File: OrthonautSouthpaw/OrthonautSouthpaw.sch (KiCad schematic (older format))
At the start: 152 parts, among them K1 7, K10 3, K11 ., K12 Tab, K13 Esc, K14 L_Shift, K15 L_Ctrl, K16 Q, K17 A, K18 Z, K19 Win, K2 4, K20 W, K21 S, K22 X, K23 L_Alt, K24 E, K25 D, K26 C, K27 Lower, K28 R, K29 F, K3 1, K30 V, K31 Space, K32 T, K33 G, K34 B, K35 Y, K36 H, K37 N, K38 U, K39 J, K4 8, K40 M, K41 Enter, K42 I, K43 K, K44 ,, K45 Raise, K46 O, K47 L, K48 ., K49 R_Alt, K5 5, K50 P, K51 ;, K52 /, K53 Fn, K54 BackSpace, K55 ', K56 R_Shift, K57 Left, K58 Insert, K59 Delete, K6 2, K60 Up, K61 Down, K62 Home, K63 End, K64 Right, K7 0, K8 9, K9 6, SW1 SW_PUSH, U1 Elite-C

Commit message: finished v1 board designed
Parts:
- removed SW1: SW_PUSH, Keebio-Parts:SW_Tactile_SPST_Angled_MJTP1117, symbol keyboard_parts:SW_PUSH
- added D4: D, Keebio-Parts:Diode-dual, symbol Device:D
- added K4: 0, Keebio-Parts:MX_PCB_100H, symbol keyboard_parts:KEYSW
- D1, D2, D3: footprint Keebio-Parts:Diode -> Keebio-Parts:Diode-dual
- D10: renamed from D9; footprint Keebio-Parts:Diode -> Keebio-Parts:Diode-dual
- D11: renamed from D10; footprint Keebio-Parts:Diode -> Keebio-Parts:Diode-dual
- D12: renamed from D11; footprint Keebio-Parts:Diode -> Keebio-Parts:Diode-dual
- D13: renamed from D12; footprint Keebio-Parts:Diode -> Keebio-Parts:Diode-dual
- D14: renamed from D13; footprint Keebio-Parts:Diode -> Keebio-Parts:Diode-dual
- D15: renamed from D14; footprint Keebio-Parts:Diode -> Keebio-Parts:Diode-dual
- D16: renamed from D15; footprint Keebio-Parts:Diode -> Keebio-Parts:Diode-dual
- D17: renamed from D16; footprint Keebio-Parts:Diode -> Keebio-Parts:Diode-dual
- D18: renamed from D17; footprint Keebio-Parts:Diode -> Keebio-Parts:Diode-dual
- D19: renamed from D18; footprint Keebio-Parts:Diode -> Keebio-Parts:Diode-dual
- D20: renamed from D19; footprint Keebio-Parts:Diode -> Keebio-Parts:Diode-dual
- D21: renamed from D20; footprint Keebio-Parts:Diode -> Keebio-Parts:Diode-dual
- D22: renamed from D21; footprint Keebio-Parts:Diode -> Keebio-Parts:Diode-dual
- D23: renamed from D22; footprint Keebio-Parts:Diode -> Keebio-Parts:Diode-dual
- D24: renamed from D23; footprint Keebio-Parts:Diode -> Keebio-Parts:Diode-dual
- D25: renamed from D28; footprint Keebio-Parts:Diode -> Keebio-Parts:Diode-dual
- D26: renamed from D29; footprint Keebio-Parts:Diode -> Keebio-Parts:Diode-dual
- D27: renamed from D30; footprint Keebio-Parts:Diode -> Keebio-Parts:Diode-dual
- D28: renamed from D31; footprint Keebio-Parts:Diode -> Keebio-Parts:Diode-dual
- D29: renamed from D32; footprint Keebio-Parts:Diode -> Keebio-Parts:Diode-dual
- D30: renamed from D33; footprint Keebio-Parts:Diode -> Keebio-Parts:Diode-dual
- D31: renamed from D34; footprint Keebio-Parts:Diode -> Keebio-Parts:Diode-dual
- D32: renamed from D35; footprint Keebio-Parts:Diode -> Keebio-Parts:Diode-dual
- D33: renamed from D40; footprint Keebio-Parts:Diode -> Keebio-Parts:Diode-dual
- D34: renamed from D41; footprint Keebio-Parts:Diode -> Keebio-Parts:Diode-dual
- D35: renamed from D42; footprint Keebio-Parts:Diode -> Keebio-Parts:Diode-dual
- D36: renamed from D47; footprint Keebio-Parts:Diode -> Keebio-Parts:Diode-dual
- D37: renamed from D48; footprint Keebio-Parts:Diode -> Keebio-Parts:Diode-dual
- D38: renamed from D49; footprint Keebio-Parts:Diode -> Keebio-Parts:Diode-dual
- D39: renamed from D50; footprint Keebio-Parts:Diode -> Keebio-Parts:Diode-dual
- D40: renamed from D51; footprint Keebio-Parts:Diode -> Keebio-Parts:Diode-dual
- D41: renamed from D52; footprint Keebio-Parts:Diode -> Keebio-Parts:Diode-dual
- D42: renamed from D53; footprint Keebio-Parts:Diode -> Keebio-Parts:Diode-dual
- D43: renamed from D58; footprint Keebio-Parts:Diode -> Keebio-Parts:Diode-dual
- D44: renamed from D59; footprint Keebio-Parts:Diode -> Keebio-Parts:Diode-dual
- D45: renamed from D60; footprint Keebio-Parts:Diode -> Keebio-Parts:Diode-dual
- D46: renamed from D61; footprint Keebio-Parts:Diode -> Keebio-Parts:Diode-dual
- D47: renamed from D62; footprint Keebio-Parts:Diode -> Keebio-Parts:Diode-dual
- D48: renamed from D63; footprint Keebio-Parts:Diode -> Keebio-Parts:Diode-dual
- D49: renamed from D64; footprint Keebio-Parts:Diode -> Keebio-Parts:Diode-dual
- D5: renamed from D4; footprint Keebio-Parts:Diode -> Keebio-Parts:Diode-dual
- D50: renamed from D65; footprint Keebio-Parts:Diode -> Keebio-Parts:Diode-dual
- D51: renamed from D66; footprint Keebio-Parts:Diode -> Keebio-Parts:Diode-dual
- D52: renamed from D67; footprint Keebio-Parts:Diode -> Keebio-Parts:Diode-dual
- D53: renamed from D68; footprint Keebio-Parts:Diode -> Keebio-Parts:Diode-dual
- D54: renamed from D69; footprint Keebio-Parts:Diode -> Keebio-Parts:Diode-dual
- D55: renamed from D70; footprint Keebio-Parts:Diode -> Keebio-Parts:Diode-dual
- D56: renamed from D71; footprint Keebio-Parts:Diode -> Keebio-Parts:Diode-dual
- D57: renamed from D72; footprint Keebio-Parts:Diode -> Keebio-Parts:Diode-dual
- D58: renamed from D73; footprint Keebio-Parts:Diode -> Keebio-Parts:Diode-dual
- D59: renamed from D74; footprint Keebio-Parts:Diode -> Keebio-Parts:Diode-dual
- D6: renamed from D5; footprint Keebio-Parts:Diode -> Keebio-Parts:Diode-dual
- D60: renamed from D75; footprint Keebio-Parts:Diode -> Keebio-Parts:Diode-dual
- D61: renamed from D76; footprint Keebio-Parts:Diode -> Keebio-Parts:Diode-dual
- D62: renamed from D77; footprint Keebio-Parts:Diode -> Keebio-Parts:Diode-dual
- D63: renamed from D78; footprint Keebio-Parts:Diode -> Keebio-Parts:Diode-dual
- D64: renamed from D79; footprint Keebio-Parts:Diode -> Keebio-Parts:Diode-dual
- D65: renamed from D80; footprint Keebio-Parts:Diode -> Keebio-Parts:Diode-dual
- D7: renamed from D6; footprint Keebio-Parts:Diode -> Keebio-Parts:Diode-dual
- D8: renamed from D7; footprint Keebio-Parts:Diode -> Keebio-Parts:Diode-dual
- D9: renamed from D8; footprint Keebio-Parts:Diode -> Keebio-Parts:Diode-dual
- H1, H2: footprint Keebio-Parts:MountingHole -> keyboard_parts:Poker_side_edge_long
- H3, H4, H5, H6: footprint Keebio-Parts:MountingHole -> keyboard_parts:Poker_oval_hole
- K8: renamed from K7; value 0 -> 00
- renumbered D24 to D66, D25 to D67, D26 to D68, D27 to D69, D36 to D70, D37 to D71, D38 to D72, D39 to D73, D43 to D74, D44 to D75, D45 to D76, D46 to D77, D54 to D78, D55 to D79, D56 to D80, D57 to D81, K9 to K10, K10 to K11, K11 to K12, K12 to K13, K13 to K14, K14 to K15, K15 to K16, K16 to K17, K17 to K18, K18 to K19, K19 to K20, K20 to K21, K21 to K22, K22 to K23, K23 to K24, K24 to K25, K25 to K26, K26 to K27, K27 to K28, K28 to K29, K29 to K30, K30 to K31, K31 to K32, K32 to K33, K33 to K34, K34 to K35, K35 to K36, K36 to K37, K37 to K38, K38 to K39, K39 to K40, K40 to K41, K41 to K42, K42 to K43, K43 to K44, K44 to K45, K45 to K46, K46 to K47, K47 to K48, K48 to K49, K4 to K5, K49 to K50, K50 to K51, K51 to K52, K52 to K53, K53 to K54, K54 to K55, K55 to K56, K56 to K57, K57 to K58, K58 to K59, K5 to K6, K59 to K60, K60 to K61, K61 to K62, K62 to K63, K63 to K64, K64 to K65, K6 to K7, K8 to K9
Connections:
- net col0: now also K4.1
- net row3: now also D4.1 (K)
- new net: D4.2 (A), K4.2
- no-connect marks 3 -> 4
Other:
- moved on the sheet: D66, D67, D68, D69, D70, D71, D72, D73, D74, D75, D76, D77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

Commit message: ordered pcb. used swillkb for case design
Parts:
- added H7, H8: Hole, keyboard_parts:Poker_oval_hole, symbol keebio:Hole
- H1, H2: footprint keyboard_parts:Poker_side_edge_long -> keyboard_parts:Poker_oval_hole
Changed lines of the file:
@@
-$EndComp
-$Comp
-L keebio:Hole H2
-U 1 1 5CE95236
-P 3400 8700
-F 0 "H2" H 3586 8753 60  0000 L CNN
-F 1 "Hole" H 3586 8647 60  0000 L CNN
-F 2 "keyboard_parts:Poker_side_edge_long" H 3400 8700 60  0001 C CNN
-F 3 "" H 3400 8700 60  0001 C CNN
-	1    3400 8700
-	1    0    0    -1
 $EndComp
 $Comp
@@
 F 3 "" H 4150 8700 60  0001 C CNN
 	1    4150 8700
-	1    0    0    -1
-$EndComp
-$Comp
-L keebio:Hole H1
-U 1 1 5CE9537A
-P 3400 8250
-F 0 "H1" H 3586 8303 60  0000 L CNN
-F 1 "Hole" H 3586 8197 60  0000 L CNN
-F 2 "keyboard_parts:Poker_side_edge_long" H 3400 8250 60  0001 C CNN
-F 3 "" H 3400 8250 60  0001 C CNN
-	1    3400 8250
 	1    0    0    -1
 $EndComp
@@
 Connection ~ 1850 2600
 NoConn ~ 2500 6850
+$Comp
+L keebio:Hole H1
+U 1 1 5CE9B221
+P 3400 7700
+F 0 "H1" H 3586 7753 60  0000 L CNN
+F 1 "Hole" H 3586 7647 60  0000 L CNN
+F 2 "keyboard_parts:Poker_oval_hole" H 3400 7700 60  0001 C CNN
+F 3 "" H 3400 7700 60  0001 C CNN
+	1    3400 7700
+	1    0    0    -1
+$EndComp
+$Comp
+L keebio:Hole H8
+U 1 1 5CE9B227
+P 4150 7700
+F 0 "H8" H 4336 7753 60  0000 L CNN
+F 1 "Hole" H 4336 7647 60  0000 L CNN
+F 2 "keyboard_parts:Poker_oval_hole" H 4150 7700 60  0001 C CNN
+F 3 "" H 4150 7700 60  0001 C CNN
+	1    4150 7700
+	1    0    0    -1
+$EndComp
+$Comp
+L keebio:Hole H7
+U 1 1 5CE9B22D
+P 4150 7200
+F 0 "H7" H 4336 7253 60  0000 L CNN
+F 1 "Hole" H 4336 7147 60  0000 L CNN
+F 2 "keyboard_parts:Poker_oval_hole" H 4150 7200 60  0001 C CNN
+F 3 "" H 4150 7200 60  0001 C CNN
+	1    4150 7200
+	1    0    0    -1
+$EndComp
+$Comp
+L keebio:Hole H2
+U 1 1 5CE9B233
+P 4150 6750
+F 0 "H2" H 4336 6803 60  0000 L CNN
+F 1 "Hole" H 4336 6697 60  0000 L CNN
+F 2 "keyboard_parts:Poker_oval_hole" H 4150 6750 60  0001 C CNN
+F 3 "" H 4150 6750 60  0001 C CNN
+	1    4150 6750
+	1    0    0    -1
+$EndComp
 $EndSCHEMATC

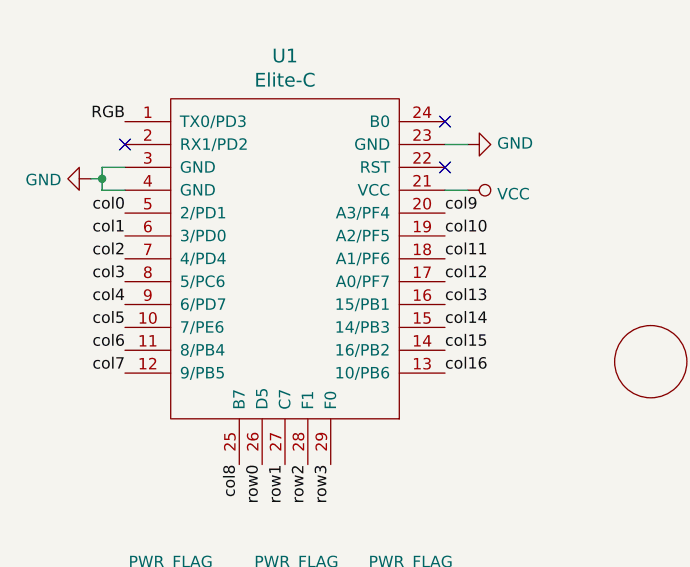
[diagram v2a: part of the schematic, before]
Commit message: update v2
v2 involves flipping the elitec component and moving it to have more space for the switch. arguably better tracing than v1
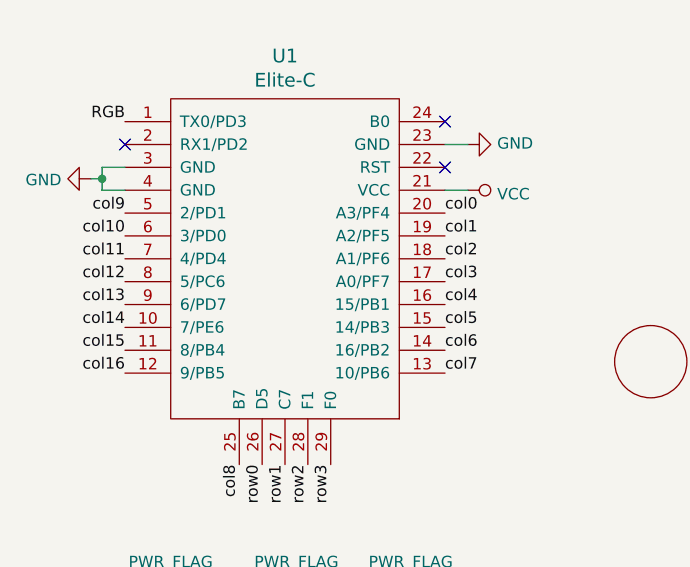
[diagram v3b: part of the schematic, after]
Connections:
- net col0: now also U1.20 (A3/PF4); no longer U1.5 (2/PD1)
- net col1: now also U1.19 (A2/PF5); no longer U1.6 (3/PD0)
- net col10: now also U1.6 (3/PD0); no longer U1.19 (A2/PF5)
- net col11: now also U1.7 (4/PD4); no longer U1.18 (A1/PF6)
- net col12: now also U1.8 (5/PC6); no longer U1.17 (A0/PF7)
- net col13: now also U1.9 (6/PD7); no longer U1.16 (15/PB1)
- net col14: now also U1.10 (7/PE6); no longer U1.15 (14/PB3)
- net col15: now also U1.11 (8/PB4); no longer U1.14 (16/PB2)
- net col16: now also U1.12 (9/PB5); no longer U1.13 (10/PB6)
- net col2: now also U1.18 (A1/PF6); no longer U1.7 (4/PD4)
- net col3: now also U1.17 (A0/PF7); no longer U1.8 (5/PC6)
- net col4: now also U1.16 (15/PB1); no longer U1.9 (6/PD7)
- net col5: now also U1.15 (14/PB3); no longer U1.10 (7/PE6)
- net col6: now also U1.14 (16/PB2); no longer U1.11 (8/PB4)
- net col7: now also U1.13 (10/PB6); no longer U1.12 (9/PB5)
- net col9: now also U1.5 (2/PD1); no longer U1.20 (A3/PF4)
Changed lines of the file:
@@
 Text Label 2000 8150 3    50   ~ 0
 row3
-Text Label 1100 7750 2    50   ~ 0
+Text Label 2500 7750 0    50   ~ 0
 col7
-Text Label 1100 7650 2    50   ~ 0
+Text Label 2500 7650 0    50   ~ 0
 col6
-Text Label 1100 7550 2    50   ~ 0
+Text Label 2500 7550 0    50   ~ 0
 col5
-Text Label 1100 7450 2    50   ~ 0
+Text Label 2500 7450 0    50   ~ 0
 col4
-Text Label 1100 7350 2    50   ~ 0
+Text Label 2500 7350 0    50   ~ 0
 col3
-Text Label 1100 7250 2    50   ~ 0
+Text Label 2500 7250 0    50   ~ 0
 col2
-Text Label 1100 7150 2    50   ~ 0
+Text Label 2500 7150 0    50   ~ 0
 col1
-Text Label 1100 7050 2    50   ~ 0
+Text Label 2500 7050 0    50   ~ 0
 col0
 Text Label 1600 8150 3    50   ~ 0
 col8
-Text Label 2500 7050 0    50   ~ 0
+Text Label 1100 7050 2    50   ~ 0
 col9
-Text Label 2500 7150 0    50   ~ 0
+Text Label 1100 7150 2    50   ~ 0
 col10
-Text Label 2500 7250 0    50   ~ 0
+Text Label 1100 7250 2    50   ~ 0
 col11
-Text Label 2500 7350 0    50   ~ 0
+Text Label 1100 7350 2    50   ~ 0
 col12
-Text Label 2500 7450 0    50   ~ 0
+Text Label 1100 7450 2    50   ~ 0
 col13
-Text Label 2500 7550 0    50   ~ 0
+Text Label 1100 7550 2    50   ~ 0
 col14
-Text Label 2500 7750 0    50   ~ 0
+Text Label 1100 7750 2    50   ~ 0
 col16
-Text Label 2500 7650 0    50   ~ 0
+Text Label 1100 7650 2    50   ~ 0
 col15
 $Comp

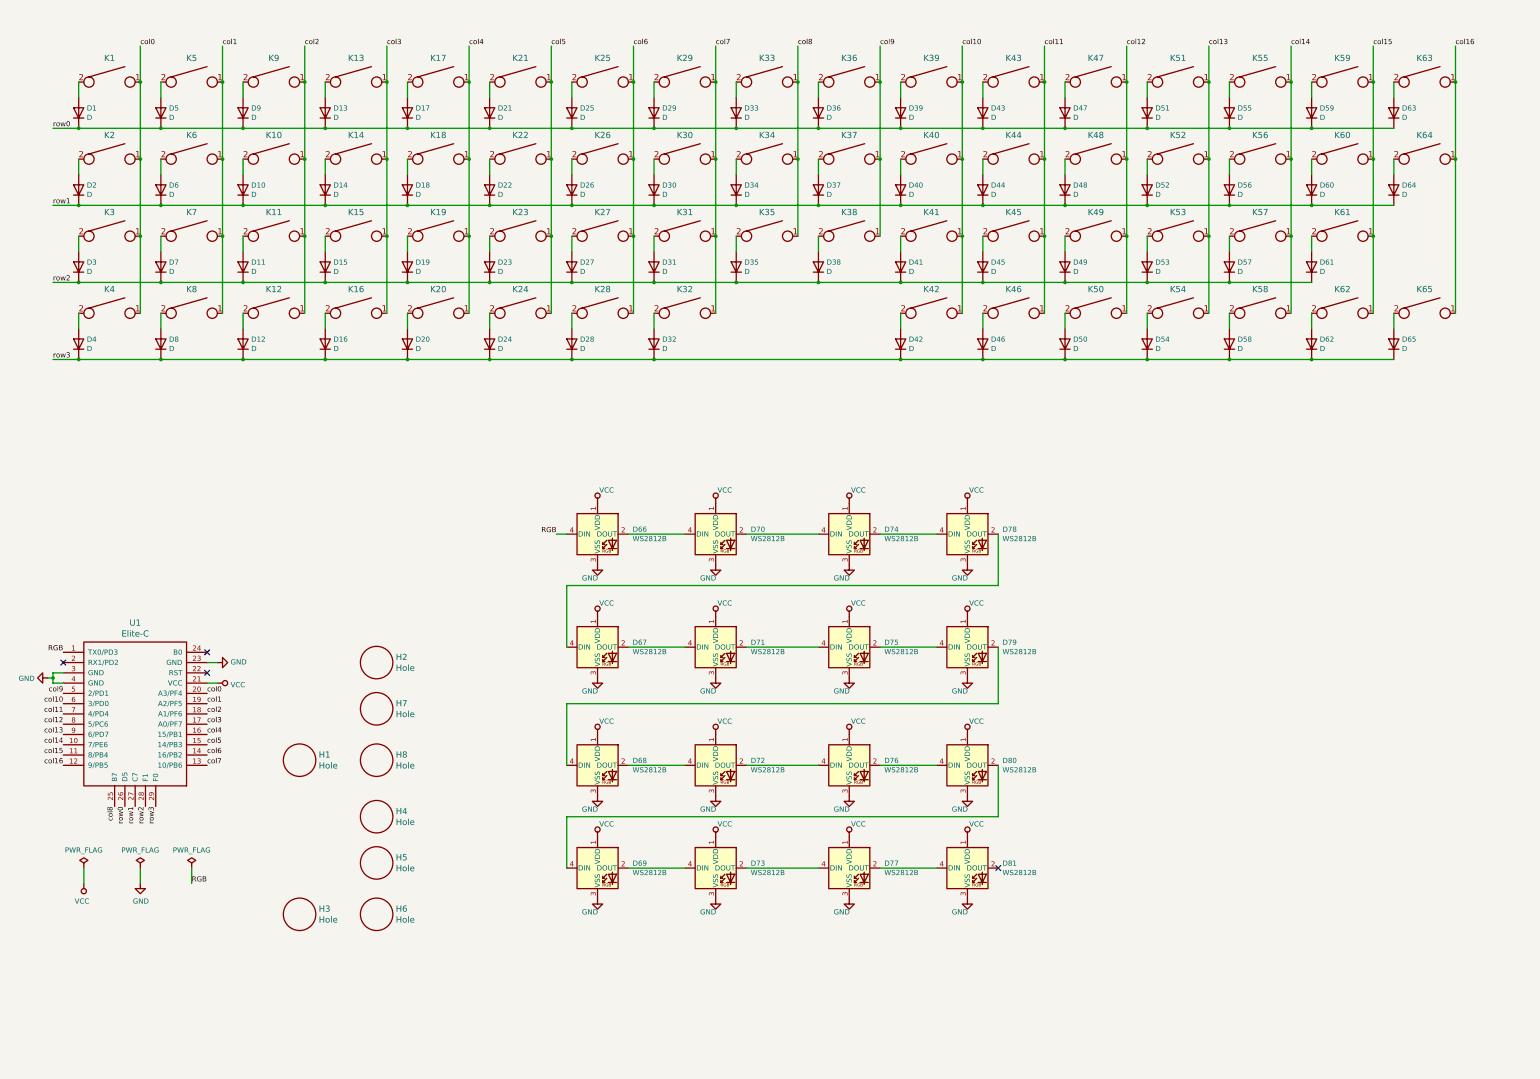
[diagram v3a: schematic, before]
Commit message: push start to v3
update to using atmega32u4. modify global libraries to project libraries. looking into type c connections to finish up schematic for atmega
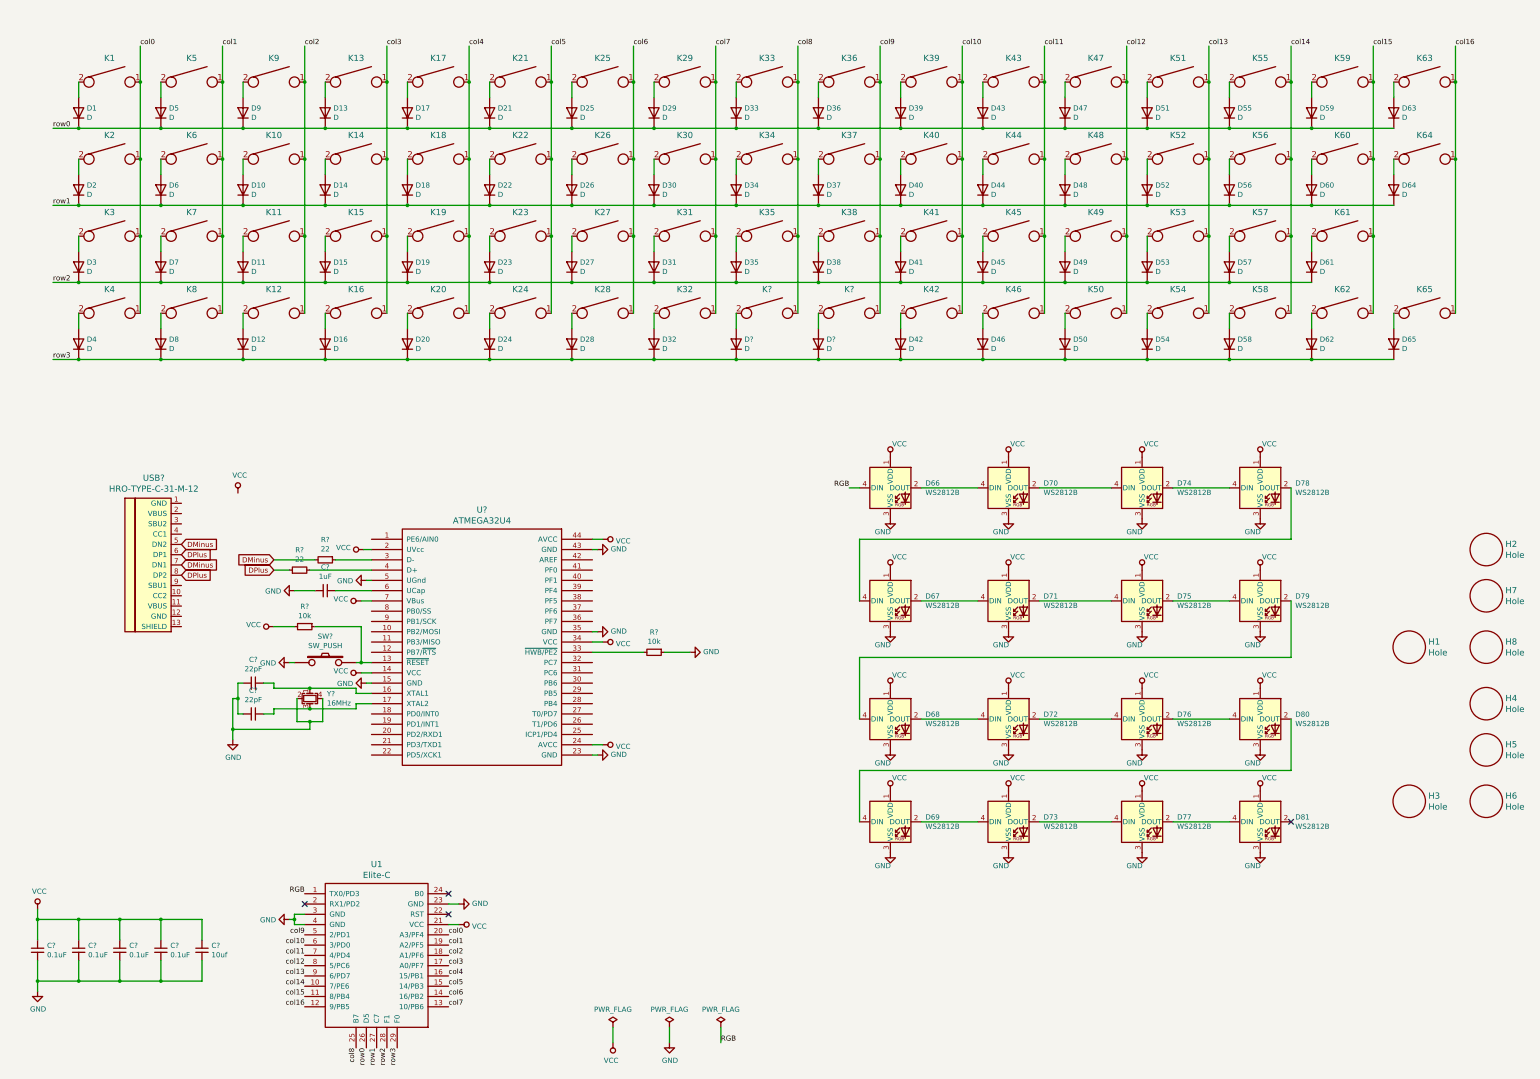
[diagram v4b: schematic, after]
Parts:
- added C? (x4): 0.1uF, symbol Device:C_Small
- added C?: 10uf, symbol Device:C_Small
- added C?: 1uF, symbol Device:C_Small
- added C? (x2): 22pF, symbol Device:C_Small
- added D? (x2): D, Keebio-Parts:Diode-dual, symbol Device:D
- added K? (x2): Space, Keebio-Parts:MX_PCB_200H, symbol keyboard_parts:KEYSW
- added R? (x2): 10k, symbol Device:R_Small
- added R? (x2): 22, symbol Device:R_Small
- added SW?: SW_PUSH, symbol keyboard_parts:SW_PUSH
- added U?: ATMEGA32U4, symbol keyboard_parts:ATMEGA32U4
- added USB?: HRO-TYPE-C-31-M-12, symbol Type-C:HRO-TYPE-C-31-M-12
- added Y?: 16MHz, symbol Device:Crystal_GND24_Small
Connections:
- net GND: now also C?.2, C?.2, C?.2, C?.2, C?.2, C?.2, C?.2, C?.2, R?.1, SW?.1, U?.15 (GND), U?.23 (GND), U?.35 (GND), U?.43 (GND), U?.5 (UGnd), Y?.2, Y?.4
- net VCC: now also C?.1, C?.1, C?.1, C?.1, C?.1, R?.2, U?.14 (VCC), U?.2 (UVcc), U?.24 (AVCC), U?.34 (VCC), U?.44 (AVCC), U?.7 (VBus)
- net col8: now also K?.1
- net col9: now also K?.1
- net row3: now also D?.1 (K), D?.1 (K)
- new net: D?.2 (A), K?.2 (x2)
- new net: R?.1, SW?.2, U?.13 (~RESET)
- new net: C?.1, U?.16 (XTAL1), Y?.1
- new net: C?.1, U?.17 (XTAL2), Y?.3
- new net: R?.1, U?.3 (D-)
- new net: R?.2, U?.33 (~HWB/PE2)
- new net: R?.2, U?.4 (D+)
- new net: C?.1, U?.6 (UCap)
- new net DMinus: R?.2, USB?.5 (DN2), USB?.7 (DN1)
- new net DPlus: R?.1, USB?.6 (DP1), USB?.8 (DP2)
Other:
- moved on the sheet: D66, D67, D68, D69, D70, D71, D72, D73, D74, D75, D76, D77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
